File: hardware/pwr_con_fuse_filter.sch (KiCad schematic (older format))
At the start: 8 parts, among them J1601 Conn_01x02, Q1601 DMP3056L, T1601 500 Ohm@100 MHz

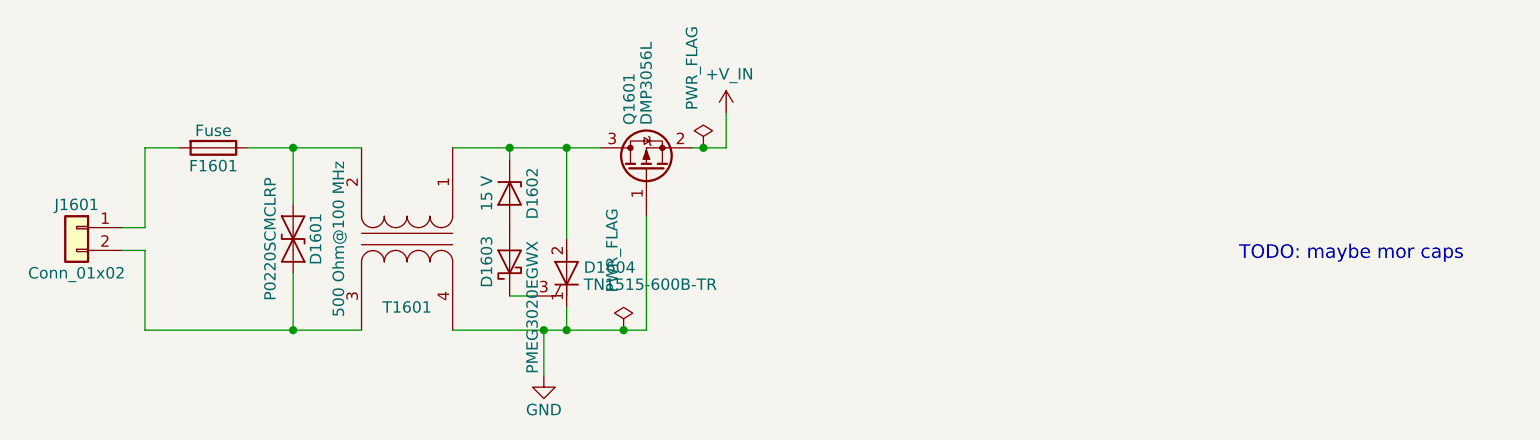
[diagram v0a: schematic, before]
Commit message: Added Step Models, fixed some footprints(e.g. added solderpaste), cleaned up a bit
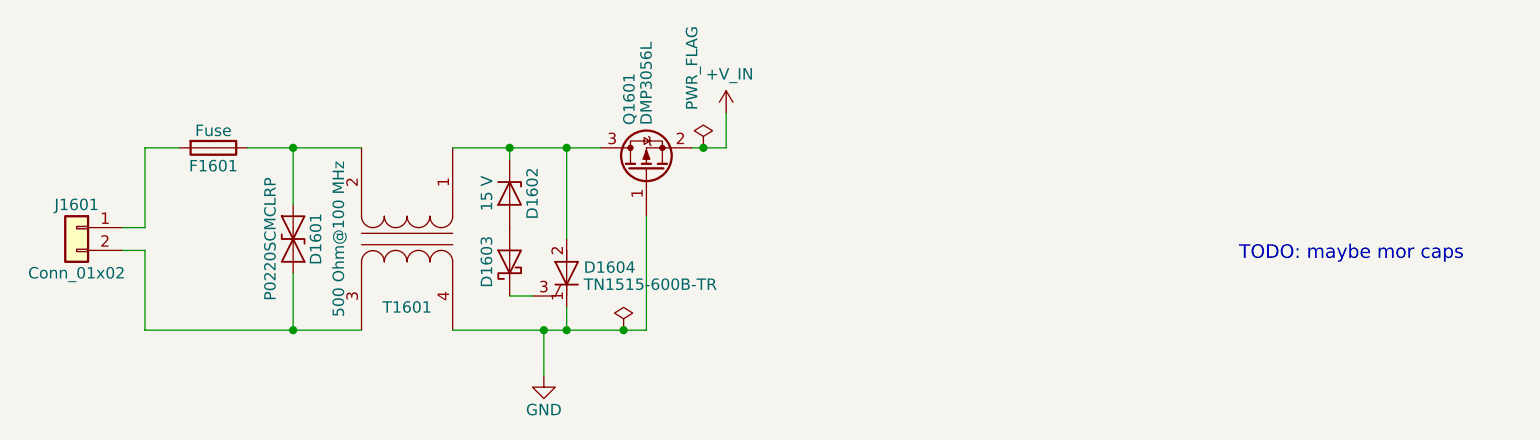
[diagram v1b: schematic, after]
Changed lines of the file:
@@
 EESchema Schematic File Version 4
 LIBS:zynq_board-cache
-EELAYER 26 0
+EELAYER 29 0
 EELAYER END
 $Descr A4 11693 8268
 encoding utf-8
-Sheet 16 21
+Sheet 14 21
 Title ""
 Date ""
@@
 P 3450 2950
 F 0 "D1603" H 3450 3050 50  0000 C CNN
-F 1 "PMEG3020EGWX" H 3250 2850 50  0000 C CNN
+F 1 "PMEG3020EGWX" H 2750 3050 50  0001 C CNN
 F 2 "Diode_SMD:D_SOD-123" H 3450 2950 50  0001 C CNN
 F 3 "https://assets.nexperia.com/documents/data-sheet/PMEG3020EGW.pdf" H 3450 2950 50  0001 C CNN
@@
 P 3950 3250
 F 0 "#FLG0101" H 3950 3325 50  0001 C CNN
-F 1 "PWR_FLAG" V 3900 3600 50  0000 C CNN
+F 1 "PWR_FLAG" V 3900 3600 50  0001 C CNN
 F 2 "" H 3950 3250 50  0001 C CNN
 F 3 "~" H 3950 3250 50  0001 C CNN
